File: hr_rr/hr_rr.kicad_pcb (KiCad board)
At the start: 2 copper layers, 41.5 x 20.5 mm, 73 parts, among them J1 Electrodes, P1 Conn_01x02_Male, P2 Conn_01x02_Male, P3 Conn_01x02_Male, Q1 DMP21D5UFB4-7B, U1 TPS62746, U2 TPS63051RMW, U3 NRF528XX-QFAA, U4 ADAS1000-4BCPZ, U6 MCP73831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

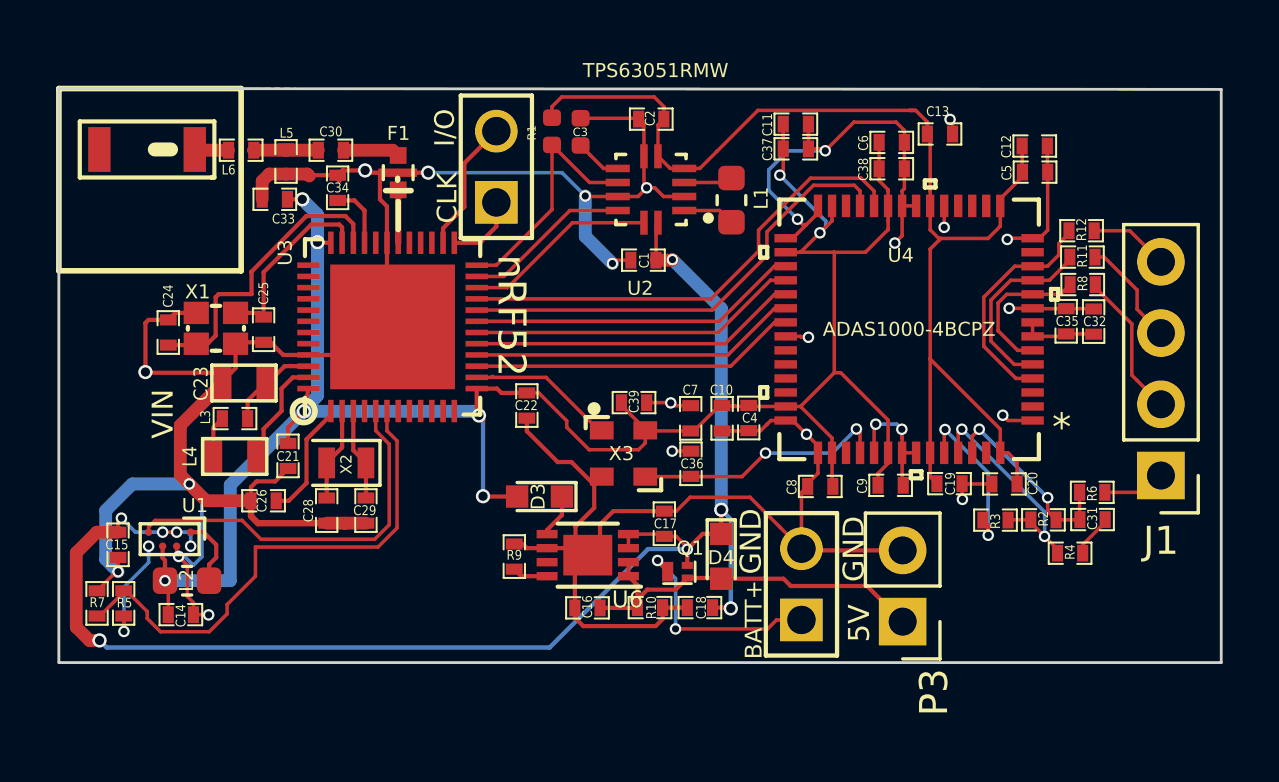
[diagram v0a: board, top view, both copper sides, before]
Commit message: Fixed via annular ring size, trace near edge.
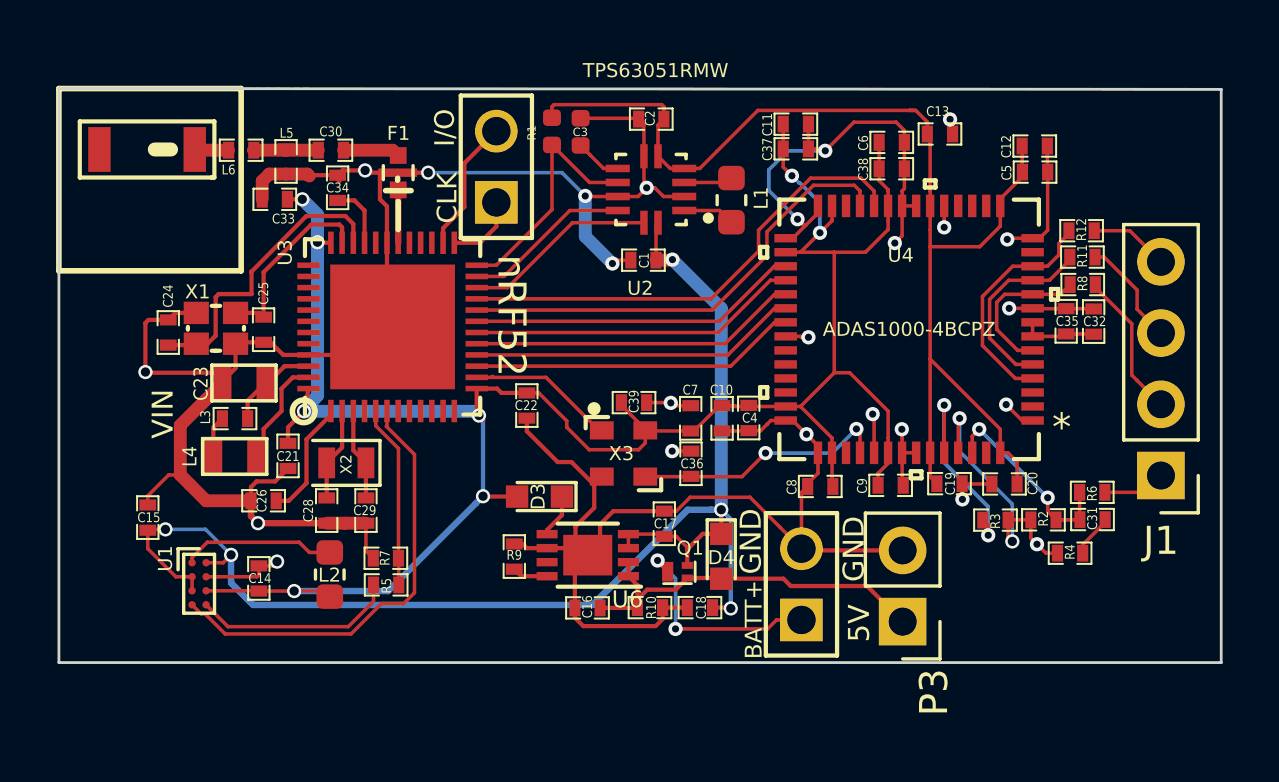
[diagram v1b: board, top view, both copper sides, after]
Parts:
- moved R7 10.4 mm to (277.6, 142.2), turned to 0 degrees
- moved R5 9.38 mm to (277.6, 143.2), turned to 0 degrees
- moved L2 5.09 mm to (275.6, 142.8), turned to 270 degrees
- moved C14 3.06 mm to (273.0, 143.0), turned to 90 degrees
- moved U1 1.91 mm to (270.9, 143.2), turned to 0 degrees
- moved C15 1.44 mm to (269.1, 140.8), turned to 90 degrees
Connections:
- U3 pad 5: /LOAD_SW_CTRL -> /AIN_BAT_DIV_VOLTAGE
- U3 pad 6: /AIN_BAT_DIV_VOLTAGE -> /LOAD_SW_CTRL
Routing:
- net /AIN_BAT_DIV_VOLTAGE: track 18.5 -> 6.54 mm
- net DGND: track 159.9 -> 151.0 mm, vias 25 -> 23
- net Vcc<BATT>: track 53.3 -> 49.4 mm, vias 9 -> 5
- net Net-(R5-Pad1): track 3.96 -> 7.26 mm, vias 2 -> 0
- net Net-(L2-Pad1): track 2.48 -> 5.47 mm
- net /LOAD_SW_CTRL: track 13.6 -> 15.9 mm
- net Net-(R2-Pad2): track 8.33 -> 10.1 mm, vias 2 -> 3
- net Net-(R3-Pad1): track 5.87 -> 7.61 mm
- net 1.8V_supply: track 78.4 -> 79.0 mm
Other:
- board text added: "nRF52-HR-RR Prototype 10/28/18 Yeo GaTech BNE Lab"
- board text removed: "nRF52-GSR Prototype 09/03/18 Yeo GaTech BNE Lab"

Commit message: (Fixed #4) CMOS Clock Reconfigure
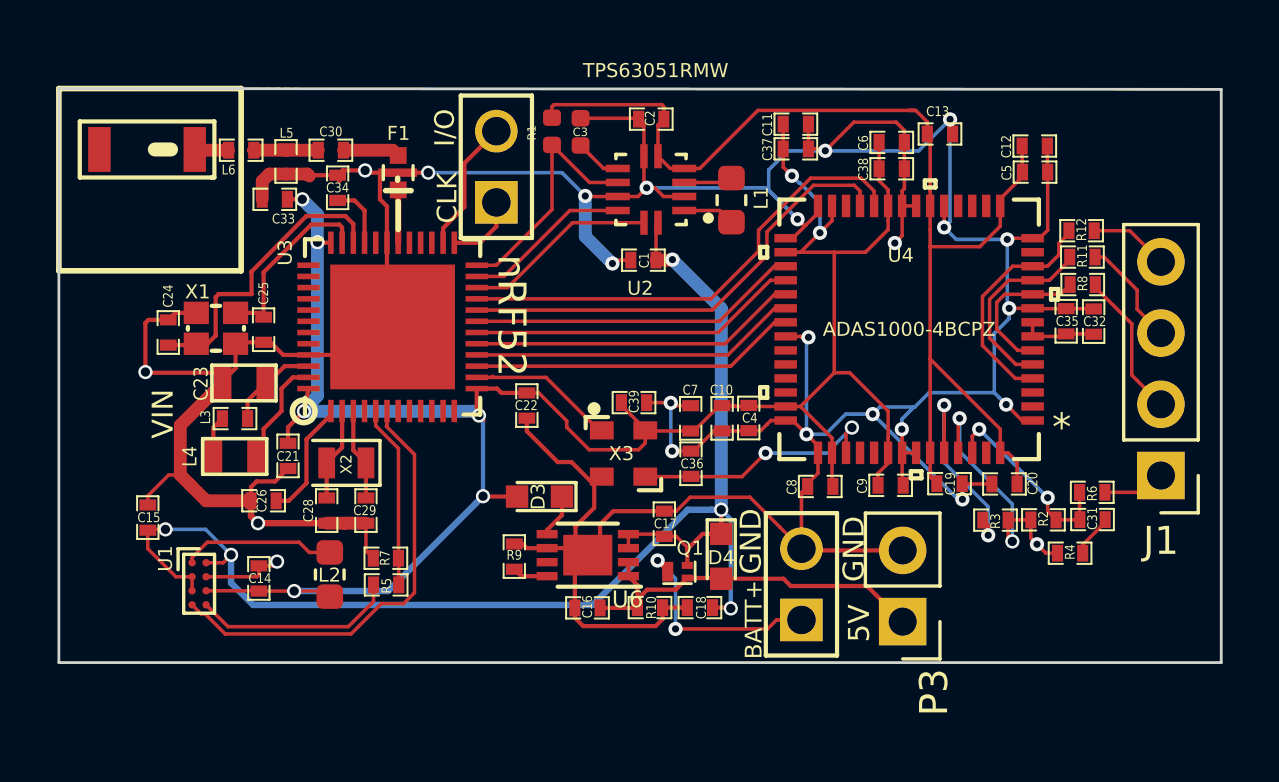
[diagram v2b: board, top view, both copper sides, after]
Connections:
- C36 pad 1: /ADAS_XTAL2 -> /DSC1001_CLK_OUT
- U4 pad 45: Net-(U4-Pad45) -> /DSC1001_CLK_OUT
- U4 pad 46: /ADAS_XTAL2 -> Net-(U4-Pad46)
- U4 pad 47: DGND -> Net-(U4-Pad47)
- X3 pad 3: /ADAS_XTAL2 -> /DSC1001_CLK_OUT
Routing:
- net DGND: track 151.0 -> 192.5 mm
- net /DSC1001_CLK_OUT: track 0.00 -> 9.20 mm, vias 0 -> 2
- net /ADAS_XTAL2: track 9.14 -> 0.00 mm, vias 2 -> 0

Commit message: (Fixed #3) Shorted EN, ILIM0 to Vcc, also removed PG from reset pin.
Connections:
- R1 pad 2: /PG_TPS63051 -> Net-(R1-Pad2)
- U2 pad 10: /ILIM0_TPS63051 -> Vcc<BATT>
- U2 pad 11: /EN_TPS63051 -> Vcc<BATT>
- U2 pad 8: /PG_TPS63051 -> Net-(R1-Pad2)
- U3 pad 22: /EN_TPS63051 -> Net-(U3-Pad22)
- U3 pad 23: /ILIM0_TPS63051 -> Net-(U3-Pad23)
- U3 pad 24: /PG_TPS63051 -> Net-(U3-Pad24)
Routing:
- net /PG_TPS63051: track 8.96 -> 0.00 mm
- net /EN_TPS63051: track 6.92 -> 0.00 mm
- net /ILIM0_TPS63051: track 6.00 -> 0.00 mm
- net Net-(R1-Pad2): track 0.00 -> 2.90 mm
- net Vcc<BATT>: track 49.4 -> 51.0 mm

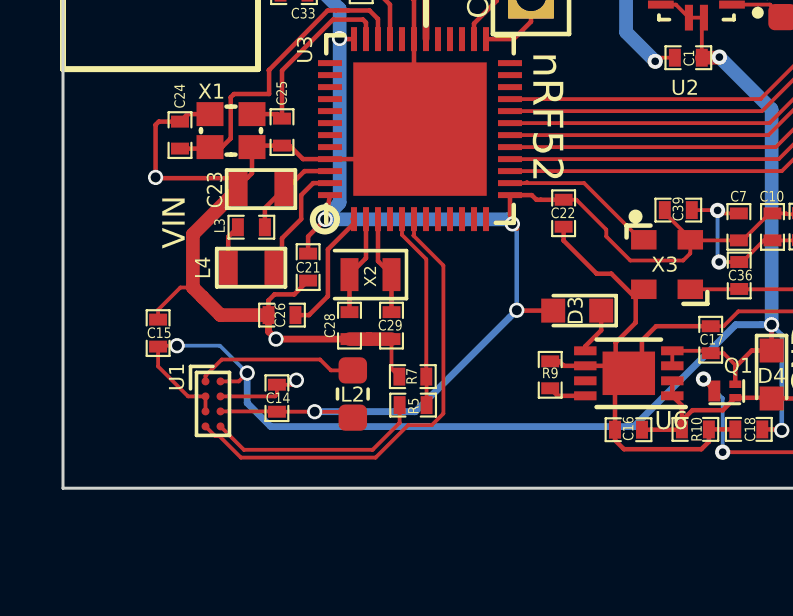
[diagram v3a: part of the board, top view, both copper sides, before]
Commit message: Fixed #2, updated BGA pattern.
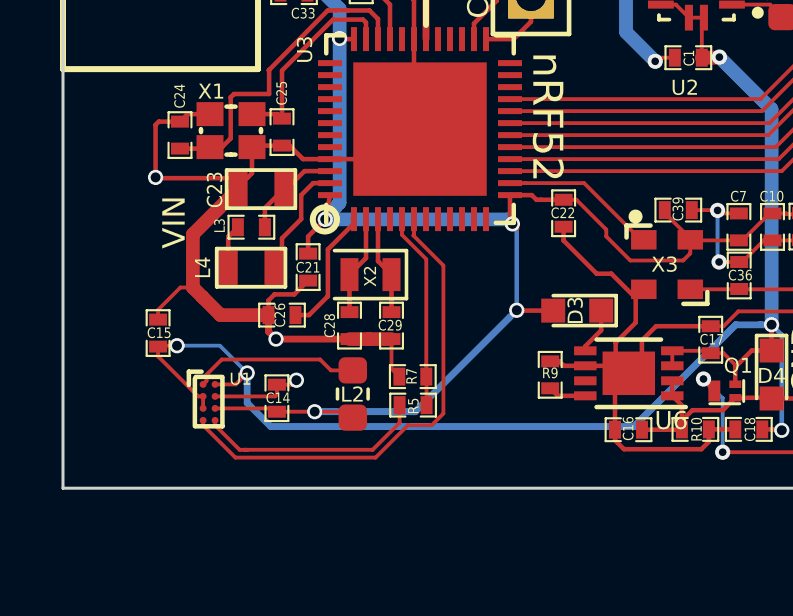
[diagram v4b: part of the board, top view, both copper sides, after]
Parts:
- U1: footprint Package_BGA:Texas_DSBGA-8_0.9x1.9mm_Layout2x4_P0.5mm -> musaPwrPad:XBGA-8
- moved U1 0.14 mm to (270.8, 143.1)
